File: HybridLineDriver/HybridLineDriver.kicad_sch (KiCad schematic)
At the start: 34 parts, among them J1 XLR3, J2 Conn_01x03, J3 Conn_01x02, U1 OPA1679

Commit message: massive pcb rework
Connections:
- net GND: now also U1.5 (+); no longer U1.12 (+)
- net at C4.1, R10.1, R12.2: now also U1.13 (-); no longer U1.6 (-)
- net at C4.2, R10.2, R13.1: now also U1.14; no longer U1.7
- net at R15.1, R20.2: now also U1.12 (+); no longer U1.5 (+)
- net at C3.2, R4.1, R9.2: now also U1.6 (-); no longer U1.13 (-)
- net at R2.1, R4.2: now also U1.7; no longer U1.14
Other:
- moved on the sheet: U1B, U1D
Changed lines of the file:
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@@
 	(symbol
 		(lib_id "Amplifier_Operational:OPA1679")
-		(at 114.3 48.26 0)
+		(at 146.05 127 0)
+		(mirror x)
 		(unit 4)
 		(exclude_from_sim no)
@@
 		(dnp no)
 		(property "Reference" "U1"
-			(at 114.3 58.42 0)
+			(at 146.05 116.84 0)
 			(effects
 				(font
@@
 		)
 		(property "Value" "OPA1679"
-			(at 114.3 55.88 0)
+			(at 146.05 119.38 0)
 			(effects
 				(font
@@
 		)
 		(property "Footprint" "Package_SO:SOIC-14_3.9x8.7mm_P1.27mm"
-			(at 113.03 45.72 0)
+			(at 144.78 129.54 0)
 			(effects
 				(font
@@
 		)
 		(property "Datasheet" "http://www.ti.com/lit/ds/symlink/opa1678.pdf"
-			(at 115.57 43.18 0)
+			(at 147.32 132.08 0)
 			(effects
 				(font
@@
 		)
 		(property "Description" "Low-Distortion Audio Operational Amplifiers, SOIC-14/TSSOP-14"
-			(at 114.3 48.26 0)
+			(at 146.05 127 0)
 			(effects
 				(font
@@
 	(symbol
 		(lib_id "Amplifier_Operational:OPA1679")
-		(at 146.05 127 0)
-		(mirror x)
+		(at 114.3 48.26 0)
 		(unit 2)
 		(exclude_from_sim no)
@@
 		(dnp no)
 		(property "Reference" "U1"
-			(at 146.05 137.16 0)
+			(at 114.3 38.1 0)
 			(effects
 				(font
@@
 		)
 		(property "Value" "OPA1679"
-			(at 146.05 134.62 0)
+			(at 114.3 40.64 0)
 			(effects
 				(font
@@
 		)
 		(property "Footprint" "Package_SO:SOIC-14_3.9x8.7mm_P1.27mm"
-			(at 144.78 129.54 0)
+			(at 113.03 45.72 0)
 			(effects
 				(font
@@
 		)
 		(property "Datasheet" "http://www.ti.com/lit/ds/symlink/opa1678.pdf"
-			(at 147.32 132.08 0)
+			(at 115.57 43.18 0)
 			(effects
 				(font
@@
 		)
 		(property "Description" "Low-Distortion Audio Operational Amplifiers, SOIC-14/TSSOP-14"
-			(at 146.05 127 0)
-			(effects
-				(font
+			(at 114.3 48.26 0)
+			(effects
+				(font

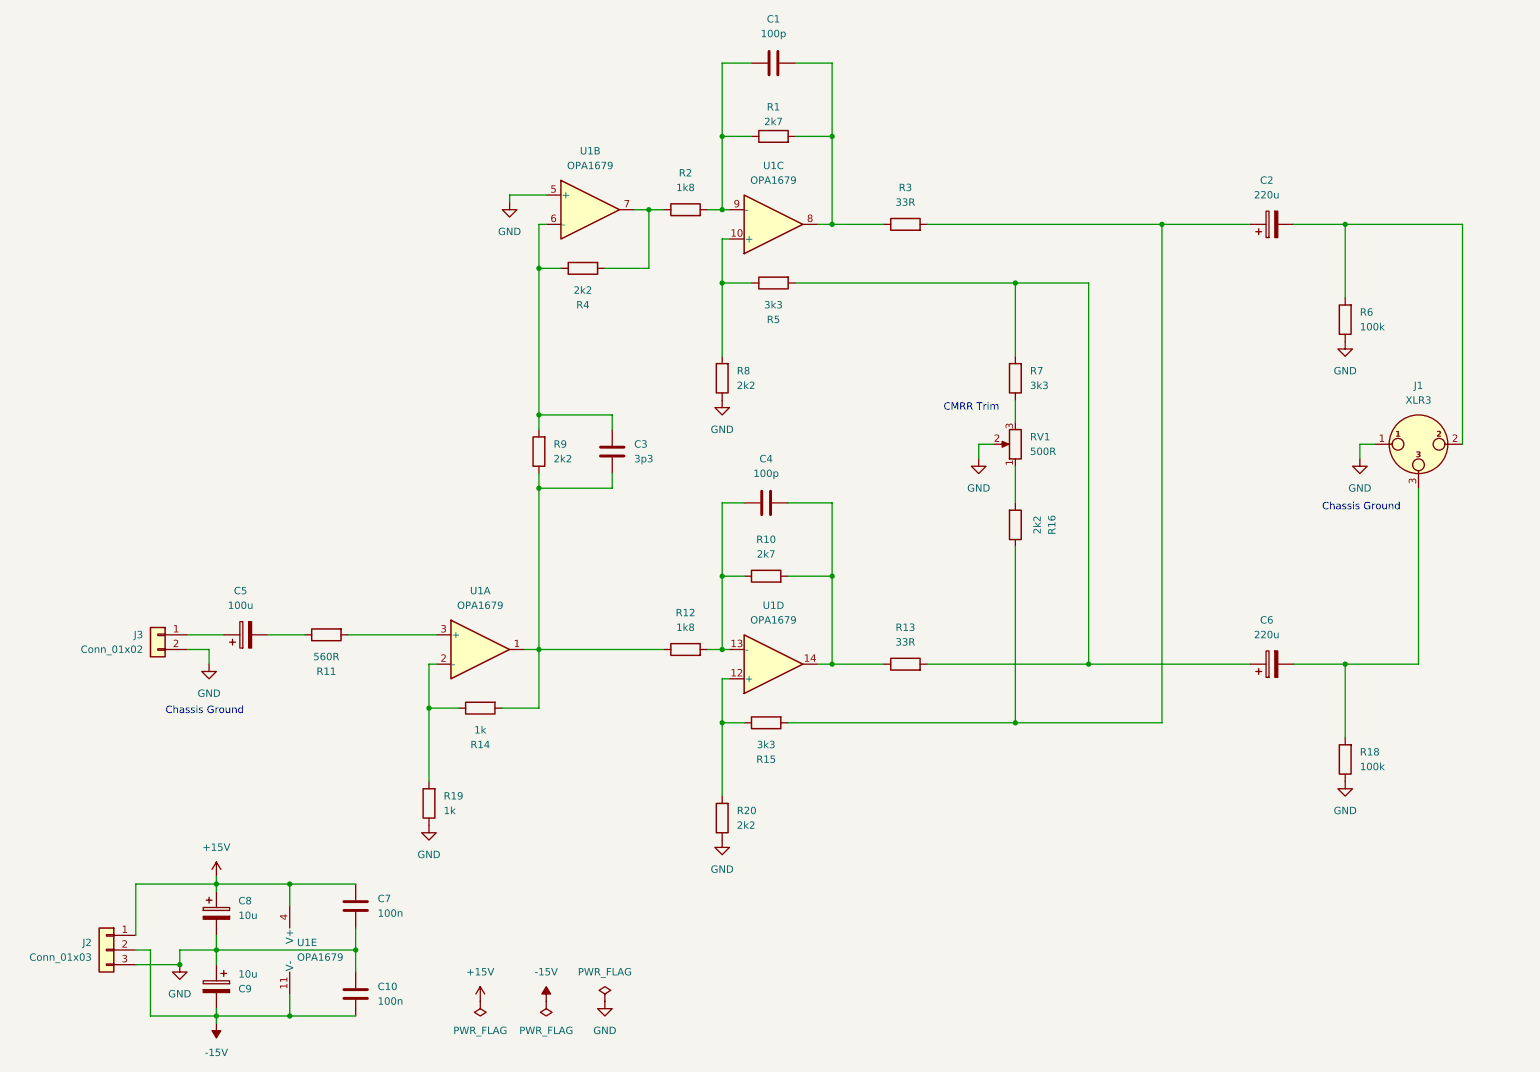
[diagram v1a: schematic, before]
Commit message: added TLA Input
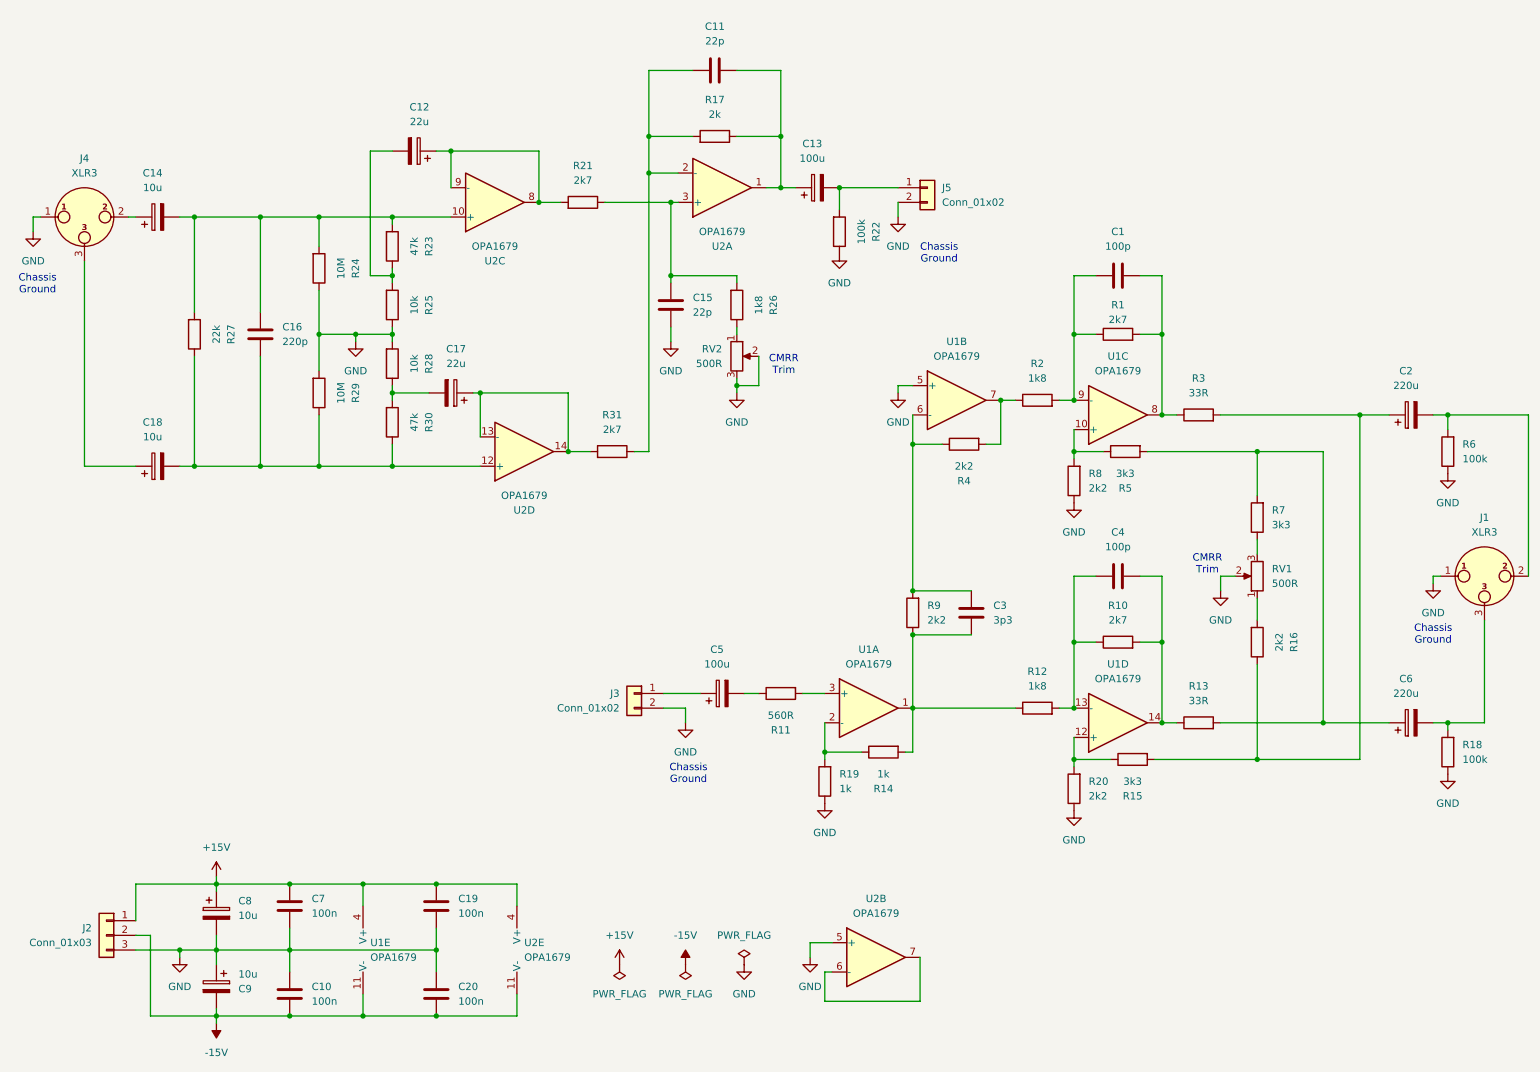
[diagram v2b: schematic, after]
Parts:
- added C11, C15: 22p, Capacitor_SMD:C_1206_3216Metric, symbol Device:C
- added C12, C17: 22u, Capacitor_THT:CP_Radial_D6.3mm_P2.50mm, symbol Device:C_Polarized
- added C13: 100u, Capacitor_THT:CP_Radial_D6.3mm_P2.50mm, symbol Device:C_Polarized
- added C14, C18: 10u, Capacitor_THT:CP_Radial_D6.3mm_P2.50mm, symbol Device:C_Polarized
- added C16: 220p, Capacitor_SMD:C_1206_3216Metric, symbol Device:C
- added C19, C20: 100n, Capacitor_SMD:C_1206_3216Metric, symbol Device:C
- added J4: XLR3, Connector_PinHeader_2.54mm:PinHeader_1x03_P2.54mm_Vertical, symbol Connector_Audio:XLR3
- added J5: Conn_01x02, Connector_PinHeader_2.54mm:PinHeader_1x02_P2.54mm_Vertical, symbol Connector_Generic:Conn_01x02
- added R17: 2k, Resistor_SMD:R_1206_3216Metric, symbol Device:R
- added R21, R31: 2k7, Resistor_SMD:R_1206_3216Metric, symbol Device:R
- added R22: 100k, Resistor_SMD:R_1206_3216Metric, symbol Device:R
- added R23, R30: 47k, Resistor_SMD:R_1206_3216Metric, symbol Device:R
- added R24, R29: 10M, Resistor_SMD:R_1206_3216Metric, symbol Device:R
- added R25, R28: 10k, Resistor_SMD:R_1206_3216Metric, symbol Device:R
- added R26: 1k8, Resistor_SMD:R_1206_3216Metric, symbol Device:R
- added R27: 22k, Resistor_SMD:R_1206_3216Metric, symbol Device:R
- added RV2: 500R, Connector_PinHeader_2.54mm:PinHeader_1x03_P2.54mm_Vertical, symbol Device:R_Potentiometer
- added U2: OPA1679, Package_SO:SOIC-14_3.9x8.7mm_P1.27mm, symbol Amplifier_Operational:OPA1679
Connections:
- net +15V: now also C19.1, U2.4 (V+)
- net -15V: now also C20.2, U2.11 (V-)
- net GND: now also C15.2, C19.2, C20.1, J4.1, J5.2 (Pin_2), R22.1, R24.1, R25.1, R28.2, R29.2, RV2.2, RV2.3, U2.5 (+)
- new net: C17.2, R28.1, R30.2
- new net: C11.1, C13.1, R17.1, U2.1
- new net: C13.2, J5.1 (Pin_1), R22.2
- new net: R26.1, RV2.1
- new net: C14.2, C16.2, R23.2, R24.2, R27.2, U2.10 (+)
- new net: C16.1, C18.2, R27.1, R29.1, R30.1, U2.12 (+)
- new net: C12.1, R21.2, U2.8, U2.9 (-)
- new net: C12.2, R23.1, R25.2
- new net: C11.2, R17.2, R31.1, U2.2 (-)
- new net: C17.1, R31.2, U2.13 (-), U2.14
- new net: C14.1, J4.2
- new net: C15.1, R21.1, R26.2, U2.3 (+)
- new net: C18.1, J4.3
- new net: U2.6 (-), U2.7
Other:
- title: Hybrid Line Driver -> TLA Input/Output
- moved on the sheet: C1, C10, C2, C3, C4, C5, C6, C7, J1, J2, J3, R1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

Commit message: added comments
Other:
- title: TLA Input/Output -> TLA Input & Output
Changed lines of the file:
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@@
 	(paper "A4")
 	(title_block
-		(title "TLA Input/Output")
+		(title "TLA Input & Output")
 		(date "2024-05-09")
-		(rev "03")
+		(rev "01")
 		(company "Greybox Audio")
 	)
